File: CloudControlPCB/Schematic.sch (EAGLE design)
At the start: 22 parts, among them J1 AUDIO_JACK_TRRSSMD_RA, U1 LPC4088FBD208, U2 SGTL5000XNLA3R2, U3 LD1117S33CTR, X1 PHB_1MM27_2X05_SNT

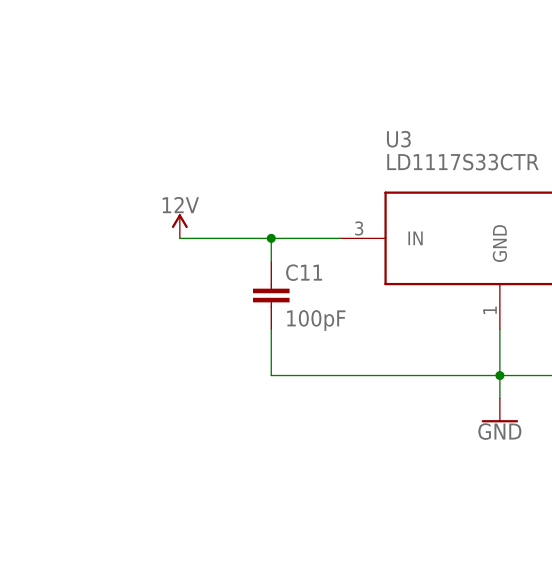
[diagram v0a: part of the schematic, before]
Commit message: add 2-pin jumper for powersupply and 3.3v regulator
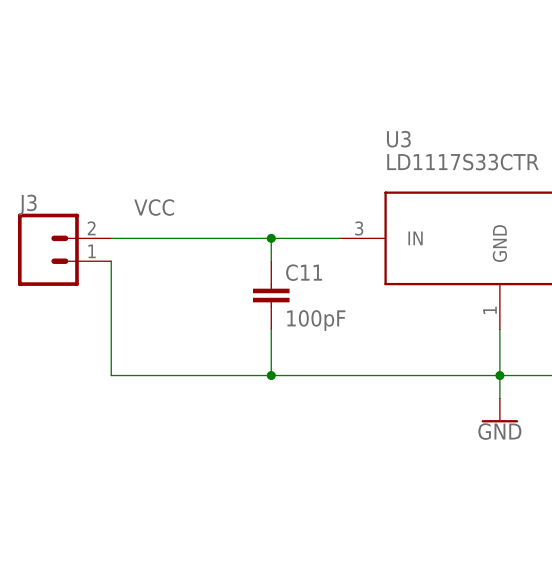
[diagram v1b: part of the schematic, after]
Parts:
- added J3: (no value), SparkFun-Connectors:CONN_02
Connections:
- removed net 12V: C11.1, U3.IN
- new net VCC: C11.1, J3.2, U3.IN
- net GND: now also J3.1
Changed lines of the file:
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@@
 <part name="GND11" library="SparkFun-PowerSymbols" library_urn="urn:adsk.eagle:library:530" deviceset="GND" device=""/>
 <part name="SUPPLY9" library="SparkFun-PowerSymbols" library_urn="urn:adsk.eagle:library:530" deviceset="3.3V" device=""/>
-<part name="SUPPLY10" library="SparkFun-PowerSymbols" library_urn="urn:adsk.eagle:library:530" deviceset="12V" device=""/>
+<part name="J3" library="SparkFun-Connectors" library_urn="urn:adsk.eagle:library:513" deviceset="CONN_02" device="" package3d_urn="urn:adsk.eagle:package:38039/1"/>
 </parts>
 <sheets>
@@
 <attribute name="VALUE" x="-71.12" y="-58.166" size="1.778" layer="96" align="bottom-center"/>
 </instance>
-<instance part="SUPPLY10" gate="G$1" x="-137.16" y="-60.96" smashed="yes">
-<attribute name="VALUE" x="-137.16" y="-58.166" size="1.778" layer="96" align="bottom-center"/>
+<instance part="J3" gate="G$1" x="-152.4" y="-63.5" smashed="yes">
+<attribute name="VALUE" x="-154.94" y="-68.326" size="1.778" layer="96" font="vector"/>
+<attribute name="NAME" x="-154.94" y="-57.912" size="1.778" layer="95" font="vector"/>
 </instance>
 </instances>
@@
 <pinref part="GND11" gate="1" pin="GND"/>
 <wire x1="-101.6" y1="-76.2" x2="-101.6" y2="-78.74" width="0.1524" layer="91"/>
+<pinref part="J3" gate="G$1" pin="1"/>
+<wire x1="-144.78" y1="-63.5" x2="-144.78" y2="-76.2" width="0.1524" layer="91"/>
+<wire x1="-144.78" y1="-76.2" x2="-127" y2="-76.2" width="0.1524" layer="91"/>
+<junction x="-127" y="-76.2"/>
 </segment>
 </net>
@@
 </segment>
 </net>
-<net name="12V" class="0">
-<segment>
-<pinref part="SUPPLY10" gate="G$1" pin="12V"/>
+<net name="VCC" class="0">
+<segment>
 <pinref part="U3" gate="G$1" pin="IN"/>
-<wire x1="-137.16" y1="-60.96" x2="-127" y2="-60.96" width="0.1524" layer="91"/>
 <pinref part="C11" gate="G$1" pin="1"/>
+<wire x1="-144.78" y1="-60.96" x2="-127" y2="-60.96" width="0.1524" layer="91"/>
 <wire x1="-127" y1="-60.96" x2="-119.38" y2="-60.96" width="0.1524" layer="91"/>
 <wire x1="-127" y1="-63.5" x2="-127" y2="-60.96" width="0.1524" layer="91"/>
 <junction x="-127" y="-60.96"/>
-</segment>
-</net>
+<pinref part="J3" gate="G$1" pin="2"/>
+<label x="-142.24" y="-58.42" size="1.778" layer="95"/>
+</segment>
+</net>

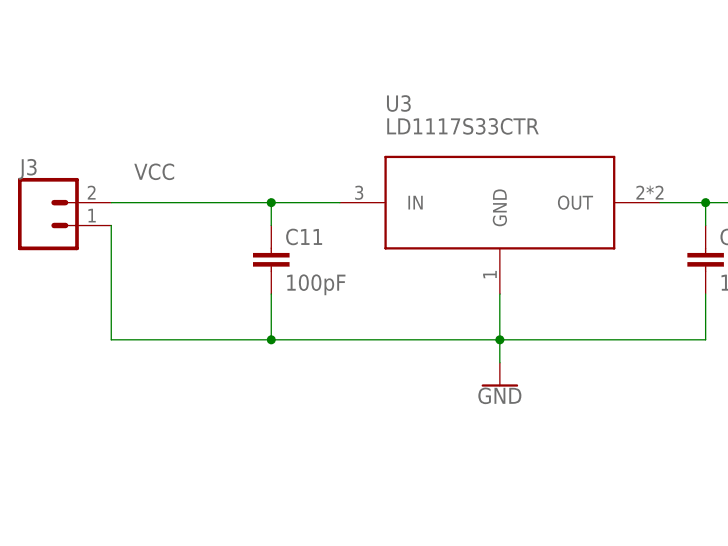
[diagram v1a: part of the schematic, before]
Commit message: Change 100pF cap to 0402 package size for regulator circuit
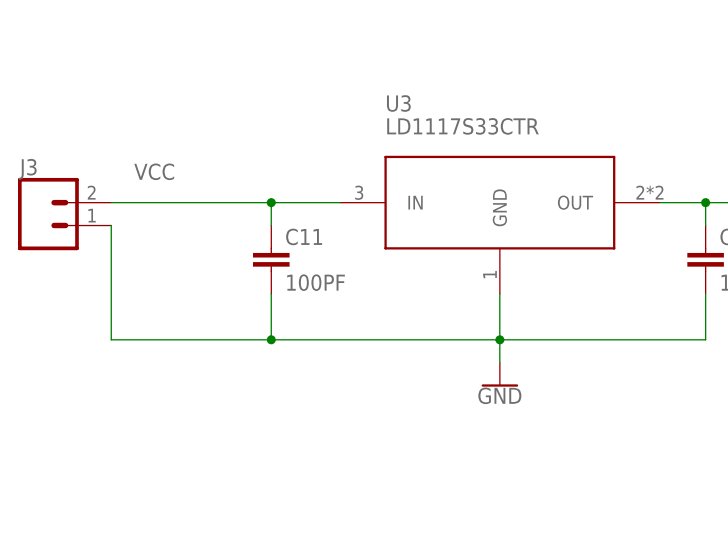
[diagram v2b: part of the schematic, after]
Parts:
- C11: value 100pF -> 100PF; device SparkFun-Capacitors:100PF-0603-50V-5% -> SparkFun-Capacitors:100PF-0402-50V-5%
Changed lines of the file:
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@@
 <part name="U3" library="LD1117S33CTR" deviceset="LD1117S33CTR" device=""/>
 <part name="C10" library="SparkFun-Capacitors" library_urn="urn:adsk.eagle:library:510" deviceset="10UF" device="-0603-6.3V-20%" package3d_urn="urn:adsk.eagle:package:37414/1" value="10uF"/>
-<part name="C11" library="SparkFun-Capacitors" library_urn="urn:adsk.eagle:library:510" deviceset="100PF" device="-0603-50V-5%" package3d_urn="urn:adsk.eagle:package:37414/1" value="100pF"/>
 <part name="GND11" library="SparkFun-PowerSymbols" library_urn="urn:adsk.eagle:library:530" deviceset="GND" device=""/>
 <part name="SUPPLY9" library="SparkFun-PowerSymbols" library_urn="urn:adsk.eagle:library:530" deviceset="3.3V" device=""/>
 <part name="J3" library="SparkFun-Connectors" library_urn="urn:adsk.eagle:library:513" deviceset="CONN_02" device="" package3d_urn="urn:adsk.eagle:package:38039/1"/>
+<part name="C11" library="SparkFun-Capacitors" library_urn="urn:adsk.eagle:library:510" deviceset="100PF" device="-0402-50V-5%" package3d_urn="urn:adsk.eagle:package:37413/1" value="100PF"/>
 </parts>
 <sheets>
@@
 <attribute name="VALUE" x="-77.216" y="-70.739" size="1.778" layer="96" font="vector"/>
 </instance>
+<instance part="GND11" gate="1" x="-101.6" y="-81.28" smashed="yes">
+<attribute name="VALUE" x="-101.6" y="-81.534" size="1.778" layer="96" align="top-center"/>
+</instance>
+<instance part="SUPPLY9" gate="G$1" x="-71.12" y="-60.96" smashed="yes">
+<attribute name="VALUE" x="-71.12" y="-58.166" size="1.778" layer="96" align="bottom-center"/>
+</instance>
+<instance part="J3" gate="G$1" x="-152.4" y="-63.5" smashed="yes">
+<attribute name="VALUE" x="-154.94" y="-68.326" size="1.778" layer="96" font="vector"/>
+<attribute name="NAME" x="-154.94" y="-57.912" size="1.778" layer="95" font="vector"/>
+</instance>
 <instance part="C11" gate="G$1" x="-127" y="-68.58" smashed="yes">
 <attribute name="NAME" x="-125.476" y="-65.659" size="1.778" layer="95" font="vector"/>
 <attribute name="VALUE" x="-125.476" y="-70.739" size="1.778" layer="96" font="vector"/>
-</instance>
-<instance part="GND11" gate="1" x="-101.6" y="-81.28" smashed="yes">
-<attribute name="VALUE" x="-101.6" y="-81.534" size="1.778" layer="96" align="top-center"/>
-</instance>
-<instance part="SUPPLY9" gate="G$1" x="-71.12" y="-60.96" smashed="yes">
-<attribute name="VALUE" x="-71.12" y="-58.166" size="1.778" layer="96" align="bottom-center"/>
-</instance>
-<instance part="J3" gate="G$1" x="-152.4" y="-63.5" smashed="yes">
-<attribute name="VALUE" x="-154.94" y="-68.326" size="1.778" layer="96" font="vector"/>
-<attribute name="NAME" x="-154.94" y="-57.912" size="1.778" layer="95" font="vector"/>
 </instance>
 </instances>
@@
 </segment>
 <segment>
-<pinref part="C11" gate="G$1" pin="2"/>
 <wire x1="-127" y1="-71.12" x2="-127" y2="-76.2" width="0.1524" layer="91"/>
 <wire x1="-127" y1="-76.2" x2="-101.6" y2="-76.2" width="0.1524" layer="91"/>
@@
 <wire x1="-144.78" y1="-76.2" x2="-127" y2="-76.2" width="0.1524" layer="91"/>
 <junction x="-127" y="-76.2"/>
+<pinref part="C11" gate="G$1" pin="2"/>
 </segment>
 </net>
@@
 <segment>
 <pinref part="U3" gate="G$1" pin="IN"/>
-<pinref part="C11" gate="G$1" pin="1"/>
 <wire x1="-144.78" y1="-60.96" x2="-127" y2="-60.96" width="0.1524" layer="91"/>
 <wire x1="-127" y1="-60.96" x2="-119.38" y2="-60.96" width="0.1524" layer="91"/>
@@
 <pinref part="J3" gate="G$1" pin="2"/>
 <label x="-142.24" y="-58.42" size="1.778" layer="95"/>
-</segment>
-</net>
+<pinref part="C11" gate="G$1" pin="1"/>
+</segment>
+</net>

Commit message: Finalize schematic
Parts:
- added C12: 10uF, SparkFun-Capacitors:10UF-0603-6.3V-20%
- added C13, C14: 18pF, SparkFun-Capacitors:18PF-0603-50V-5%
- added J4: (no value), SparkFun-Connectors:CONN_02
- added U$1: SOT230P700X180-4N, SOT230P700X180-4N:SOT230P700X180-4N
- added U$2: XTAL_FA-238_25.0000MB-C3, XTAL_FA-238_25.0000MB-C3:XTAL_FA-238_25.0000MB-C3
- C11: value 100PF -> 0.1uF; device SparkFun-Capacitors:100PF-0402-50V-5% -> SparkFun-Capacitors:0.1UF-0603-25V-(+80/-20%)
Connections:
- removed net 1.8V: C4.1, C5.1, C6.1, U2.VDDA, U2.VDDIO
- removed net EARTH: J1.EARTH
- new net N$18: J4.2, U1.!RESET!
- new net N$19: C13.1, U$2.OUT, U1.XTAL2
- new net N$20: C12.1, C4.1, C5.1, C6.1, U$1.OUT, U2.VDDA, U2.VDDD, U2.VDDIO
- net GND: now also C12.2, C13.2, C14.2, C4.2, C5.2, C6.2, J4.1, U$1.GND, U$2.GND
- net N$3: now also C14.1, U$2.VCC, U1.XTAL1; no longer U2.VDDD
- net VCC: now also U$1.IN
